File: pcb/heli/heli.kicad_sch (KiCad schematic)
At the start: 34 parts, among them J1 Batterie, J2 Debug, J3 Radio, Q1 IRLZ44N, U1 AZ1117-3.3, U2 STM32F103CBTx

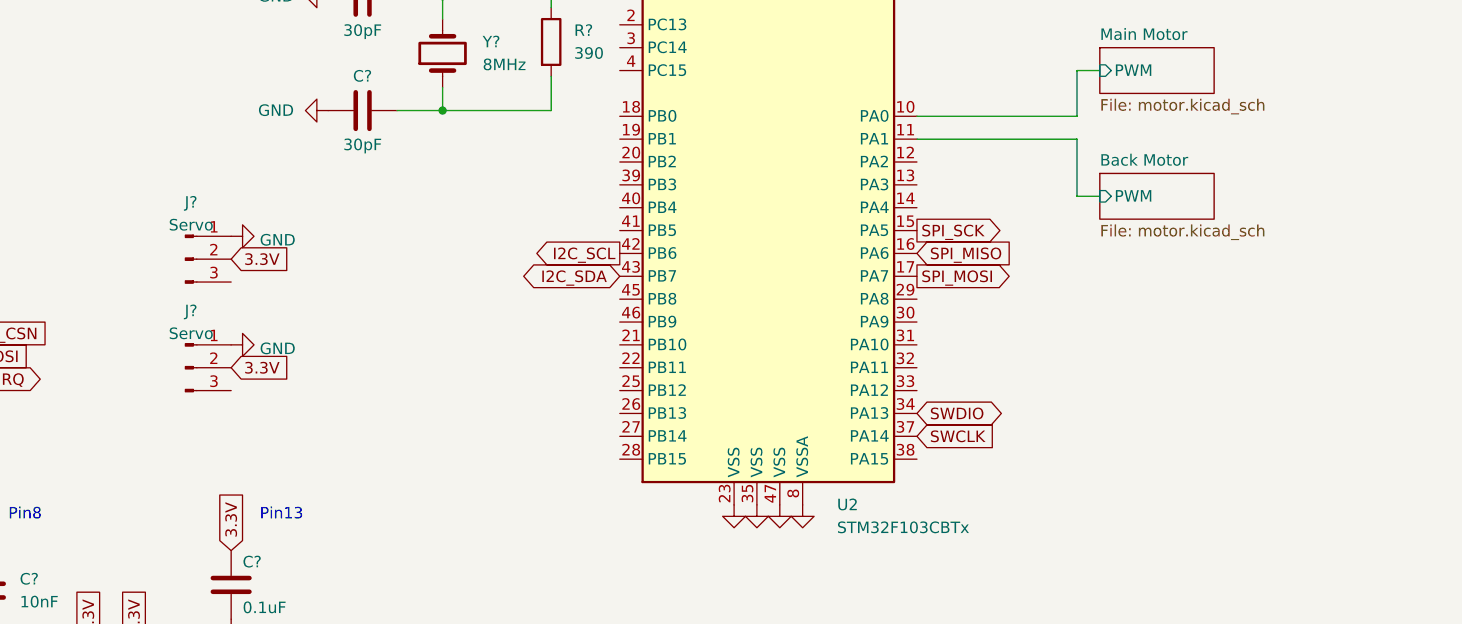
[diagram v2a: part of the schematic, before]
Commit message: 
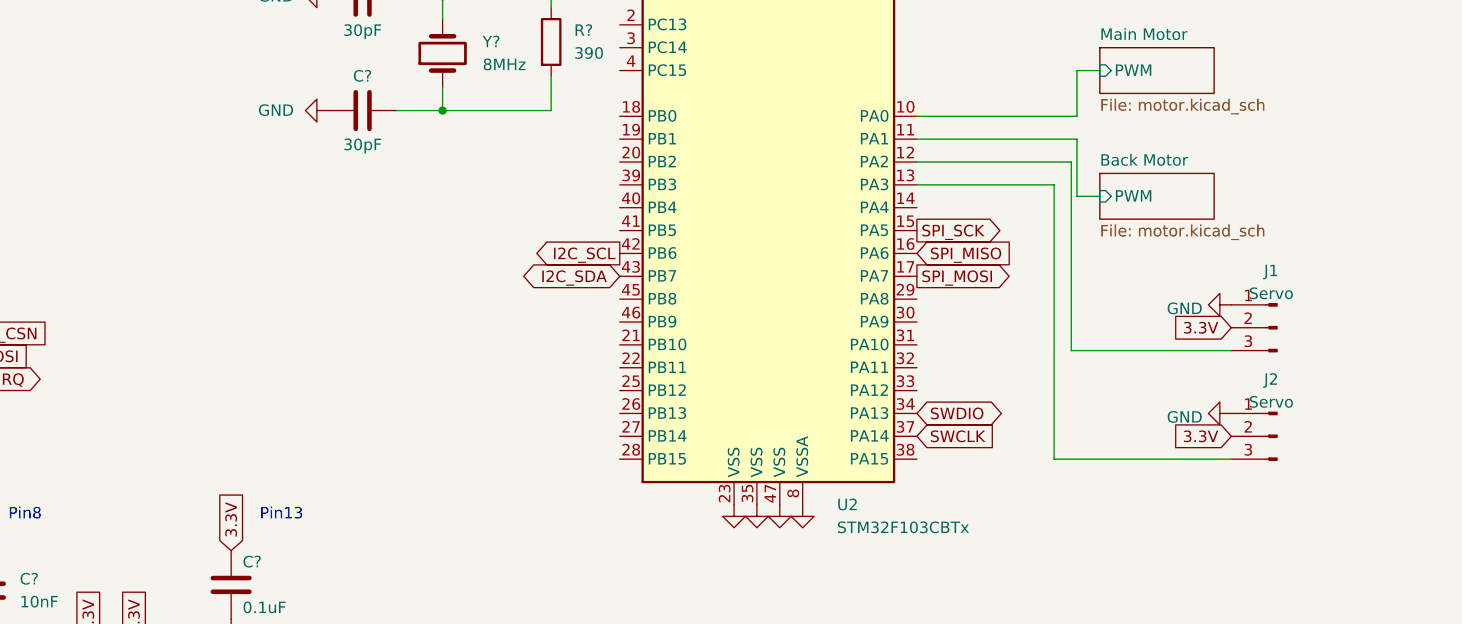
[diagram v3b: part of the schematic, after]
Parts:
- gave numbers to parts that had none: 2
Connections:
- net at U2.12 (PA2): now also J1.3 (Pin_3)
- net at U2.13 (PA3): now also J2.3 (Pin_3)
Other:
- moved on the sheet: J1, J2
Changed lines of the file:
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@@
+    (stroke (width 0) (type default) (color 0 0 0 0))
+  )
+  (wire (pts (xy 194.31 93.98) (xy 209.55 93.98))
     (stroke (width 0) (type default) (color 0 0 0 0))
   )
@@
     (stroke (width 0) (type default) (color 0 0 0 0))
   )
+  (wire (pts (xy 209.55 93.98) (xy 209.55 124.46))
+    (stroke (width 0) (type default) (color 0 0 0 0))
+  )
   (wire (pts (xy 38.1 55.88) (xy 45.72 55.88))
     (stroke (width 0) (type default) (color 0 0 0 0))
@@
     (stroke (width 0) (type default) (color 0 0 0 0))
   )
+  (wire (pts (xy 194.31 91.44) (xy 211.455 91.44))
+    (stroke (width 0) (type default) (color 0 0 0 0))
+  )
   (wire (pts (xy 245.11 39.37) (xy 245.11 34.29))
     (stroke (width 0) (type default) (color 0 0 0 0))
@@
     (stroke (width 0) (type default) (color 0 0 0 0))
   )
+  (wire (pts (xy 211.455 112.395) (xy 229.235 112.395))
+    (stroke (width 0) (type default) (color 0 0 0 0))
+  )
   (wire (pts (xy 104.14 36.83) (xy 113.03 36.83))
     (stroke (width 0) (type default) (color 0 0 0 0))
@@
     (stroke (width 0) (type default) (color 0 0 0 0))
   )
+  (wire (pts (xy 211.455 91.44) (xy 211.455 112.395))
+    (stroke (width 0) (type default) (color 0 0 0 0))
+  )
   (wire (pts (xy 141.605 75.565) (xy 141.605 73.025))
     (stroke (width 0) (type default) (color 0 0 0 0))
@@
   )
   (wire (pts (xy 33.02 67.31) (xy 29.21 67.31))
+    (stroke (width 0) (type default) (color 0 0 0 0))
+  )
+  (wire (pts (xy 209.55 124.46) (xy 229.235 124.46))
     (stroke (width 0) (type default) (color 0 0 0 0))
   )
@@
     )
   )
-  (global_label "3.3V" (shape input) (at 118.11 114.3 0) (fields_autoplaced)
-    (effects (font (size 1.27 1.27)) (justify left))
-    (property "Intersheet References" "${INTERSHEET_REFS}" (id 0) (at 124.6355 114.2206 0)
-      (effects (font (size 1.27 1.27)) (justify left) hide)
+  (global_label "3.3V" (shape input) (at 229.235 121.92 180) (fields_autoplaced)
+    (effects (font (size 1.27 1.27)) (justify right))
+    (property "Intersheet References" "${INTERSHEET_REFS}" (id 0) (at 222.7095 121.8406 0)
+      (effects (font (size 1.27 1.27)) (justify right) hide)
     )
   )
@@
     )
   )
-  (global_label "3.3V" (shape input) (at 118.11 102.235 0) (fields_autoplaced)
-    (effects (font (size 1.27 1.27)) (justify left))
-    (property "Intersheet References" "${INTERSHEET_REFS}" (id 0) (at 124.6355 102.1556 0)
-      (effects (font (size 1.27 1.27)) (justify left) hide)
+  (global_label "3.3V" (shape input) (at 229.235 109.855 180) (fields_autoplaced)
+    (effects (font (size 1.27 1.27)) (justify right))
+    (property "Intersheet References" "${INTERSHEET_REFS}" (id 0) (at 222.7095 109.7756 0)
+      (effects (font (size 1.27 1.27)) (justify right) hide)
     )
   )
@@
     (pin "9")
   )
-  (symbol (lib_id "Connector:Conn_01x03_Male") (at 113.03 114.3 0) (unit 1)
-    (in_bom yes) (on_board yes) (fields_autoplaced)
-    (property "Reference" "J?" (id 0) (at 113.665 107.984 0))
-    (property "Value" "Servo" (id 1) (at 113.665 110.5209 0))
-    (property "Footprint" "Connector_PinHeader_2.54mm:PinHeader_1x03_P2.54mm_Vertical" (id 2) (at 113.03 114.3 0)
-      (effects (font (size 1.27 1.27)) hide)
-    )
-    (property "Datasheet" "~" (id 3) (at 113.03 114.3 0)
+  (symbol (lib_id "Connector:Conn_01x03_Male") (at 234.315 121.92 0) (mirror y) (unit 1)
+    (in_bom yes) (on_board yes) (fields_autoplaced)
+    (property "Reference" "J2" (id 0) (at 233.68 115.604 0))
+    (property "Value" "Servo" (id 1) (at 233.68 118.1409 0))
+    (property "Footprint" "Connector_PinHeader_2.54mm:PinHeader_1x03_P2.54mm_Vertical" (id 2) (at 234.315 121.92 0)
+      (effects (font (size 1.27 1.27)) hide)
+    )
+    (property "Datasheet" "~" (id 3) (at 234.315 121.92 0)
       (effects (font (size 1.27 1.27)) hide)
     )
@@
     (pin "1")
   )
-  (symbol (lib_id "Connector:Conn_01x03_Male") (at 113.03 102.235 0) (unit 1)
-    (in_bom yes) (on_board yes) (fields_autoplaced)
-    (property "Reference" "J?" (id 0) (at 113.665 95.919 0))
-    (property "Value" "Servo" (id 1) (at 113.665 98.4559 0))
-    (property "Footprint" "Connector_PinHeader_2.54mm:PinHeader_1x03_P2.54mm_Vertical" (id 2) (at 113.03 102.235 0)
-      (effects (font (size 1.27 1.27)) hide)
-    )
-    (property "Datasheet" "~" (id 3) (at 113.03 102.235 0)
+  (symbol (lib_id "Connector:Conn_01x03_Male") (at 234.315 109.855 0) (mirror y) (unit 1)
+    (in_bom yes) (on_board yes) (fields_autoplaced)
+    (property "Reference" "J1" (id 0) (at 233.68 103.539 0))
+    (property "Value" "Servo" (id 1) (at 233.68 106.0759 0))
+    (property "Footprint" "Connector_PinHeader_2.54mm:PinHeader_1x03_P2.54mm_Vertical" (id 2) (at 234.315 109.855 0)
+      (effects (font (size 1.27 1.27)) hide)
+    )
+    (property "Datasheet" "~" (id 3) (at 234.315 109.855 0)
       (effects (font (size 1.27 1.27)) hide)
     )
@@
     (pin "2")
   )
-  (symbol (lib_id "power:GND") (at 118.11 99.695 90) (unit 1)
-    (in_bom yes) (on_board yes) (fields_autoplaced)
-    (property "Reference" "#PWR0130" (id 0) (at 124.46 99.695 0)
-      (effects (font (size 1.27 1.27)) hide)
-    )
-    (property "Value" "GND" (id 1) (at 121.285 100.1288 90)
+  (symbol (lib_id "power:GND") (at 229.235 107.315 270) (mirror x) (unit 1)
+    (in_bom yes) (on_board yes) (fields_autoplaced)
+    (property "Reference" "#PWR0130" (id 0) (at 222.885 107.315 0)
+      (effects (font (size 1.27 1.27)) hide)
+    )
+    (property "Value" "GND" (id 1) (at 226.06 107.7488 90)
       (effects (font (size 1.27 1.27)) (justify right))
     )
-    (property "Footprint" "" (id 2) (at 118.11 99.695 0)
-      (effects (font (size 1.27 1.27)) hide)
-    )
-    (property "Datasheet" "" (id 3) (at 118.11 99.695 0)
+    (property "Footprint" "" (id 2) (at 229.235 107.315 0)
+      (effects (font (size 1.27 1.27)) hide)
+    )
+    (property "Datasheet" "" (id 3) (at 229.235 107.315 0)
       (effects (font (size 1.27 1.27)) hide)
     )
@@
     (pin "2")
   )
-  (symbol (lib_id "power:GND") (at 118.11 111.76 90) (unit 1)
-    (in_bom yes) (on_board yes) (fields_autoplaced)
-    (property "Reference" "#PWR0129" (id 0) (at 124.46 111.76 0)
-      (effects (font (size 1.27 1.27)) hide)
-    )
-    (property "Value" "GND" (id 1) (at 121.285 112.1938 90)
+  (symbol (lib_id "power:GND") (at 229.235 119.38 270) (mirror x) (unit 1)
+    (in_bom yes) (on_board yes) (fields_autoplaced)
+    (property "Reference" "#PWR0129" (id 0) (at 222.885 119.38 0)
+      (effects (font (size 1.27 1.27)) hide)
+    )
+    (property "Value" "GND" (id 1) (at 226.06 119.8138 90)
       (effects (font (size 1.27 1.27)) (justify right))
     )
-    (property "Footprint" "" (id 2) (at 118.11 111.76 0)
-      (effects (font (size 1.27 1.27)) hide)
-    )
-    (property "Datasheet" "" (id 3) (at 118.11 111.76 0)
+    (property "Footprint" "" (id 2) (at 229.235 119.38 0)
+      (effects (font (size 1.27 1.27)) hide)
+    )
+    (property "Datasheet" "" (id 3) (at 229.235 119.38 0)
       (effects (font (size 1.27 1.27)) hide)
     )
@@
       (reference "D?") (unit 1) (value "LED") (footprint "LED_SMD:LED_0603_1608Metric")
     )
+    (path "/6a616114-ec84-4df9-9c86-6292a01164f6"
+      (reference "J1") (unit 1) (value "Servo") (footprint "Connector_PinHeader_2.54mm:PinHeader_1x03_P2.54mm_Vertical")
+    )
     (path "/7343ee5a-7884-4dc9-ac03-cc5d5c203894"
       (reference "J1") (unit 1) (value "Batterie") (footprint "Connector_PinHeader_2.54mm:PinHeader_1x02_P2.54mm_Horizontal")
     )
+    (path "/629d9c9a-835c-4513-b36f-084bde0489e8"
+      (reference "J2") (unit 1) (value "Servo") (footprint "Connector_PinHeader_2.54mm:PinHeader_1x03_P2.54mm_Vertical")
+    )
     (path "/a572e332-5d04-4c16-ab49-7a7eb34c0212"
       (reference "J2") (unit 1) (value "Debug") (footprint "Connector_PinHeader_2.54mm:PinHeader_1x05_P2.54mm_Vertical")
@@
       (reference "J3") (unit 1) (value "Radio") (footprint "Connector_PinHeader_2.54mm:PinHeader_2x04_P2.54mm_Vertical")
     )
-    (path "/629d9c9a-835c-4513-b36f-084bde0489e8"
-      (reference "J?") (unit 1) (value "Servo") (footprint "Connector_PinHeader_2.54mm:PinHeader_1x03_P2.54mm_Vertical")
-    )
-    (path "/6a616114-ec84-4df9-9c86-6292a01164f6"
-      (reference "J?") (unit 1) (value "Servo") (footprint "Connector_PinHeader_2.54mm:PinHeader_1x03_P2.54mm_Vertical")
-    )
     (path "/c5583cdf-ca59-48f7-a91f-20c1806ad1c1/ea2bd08c-49e2-43b8-8c1f-a2b101dfb062"

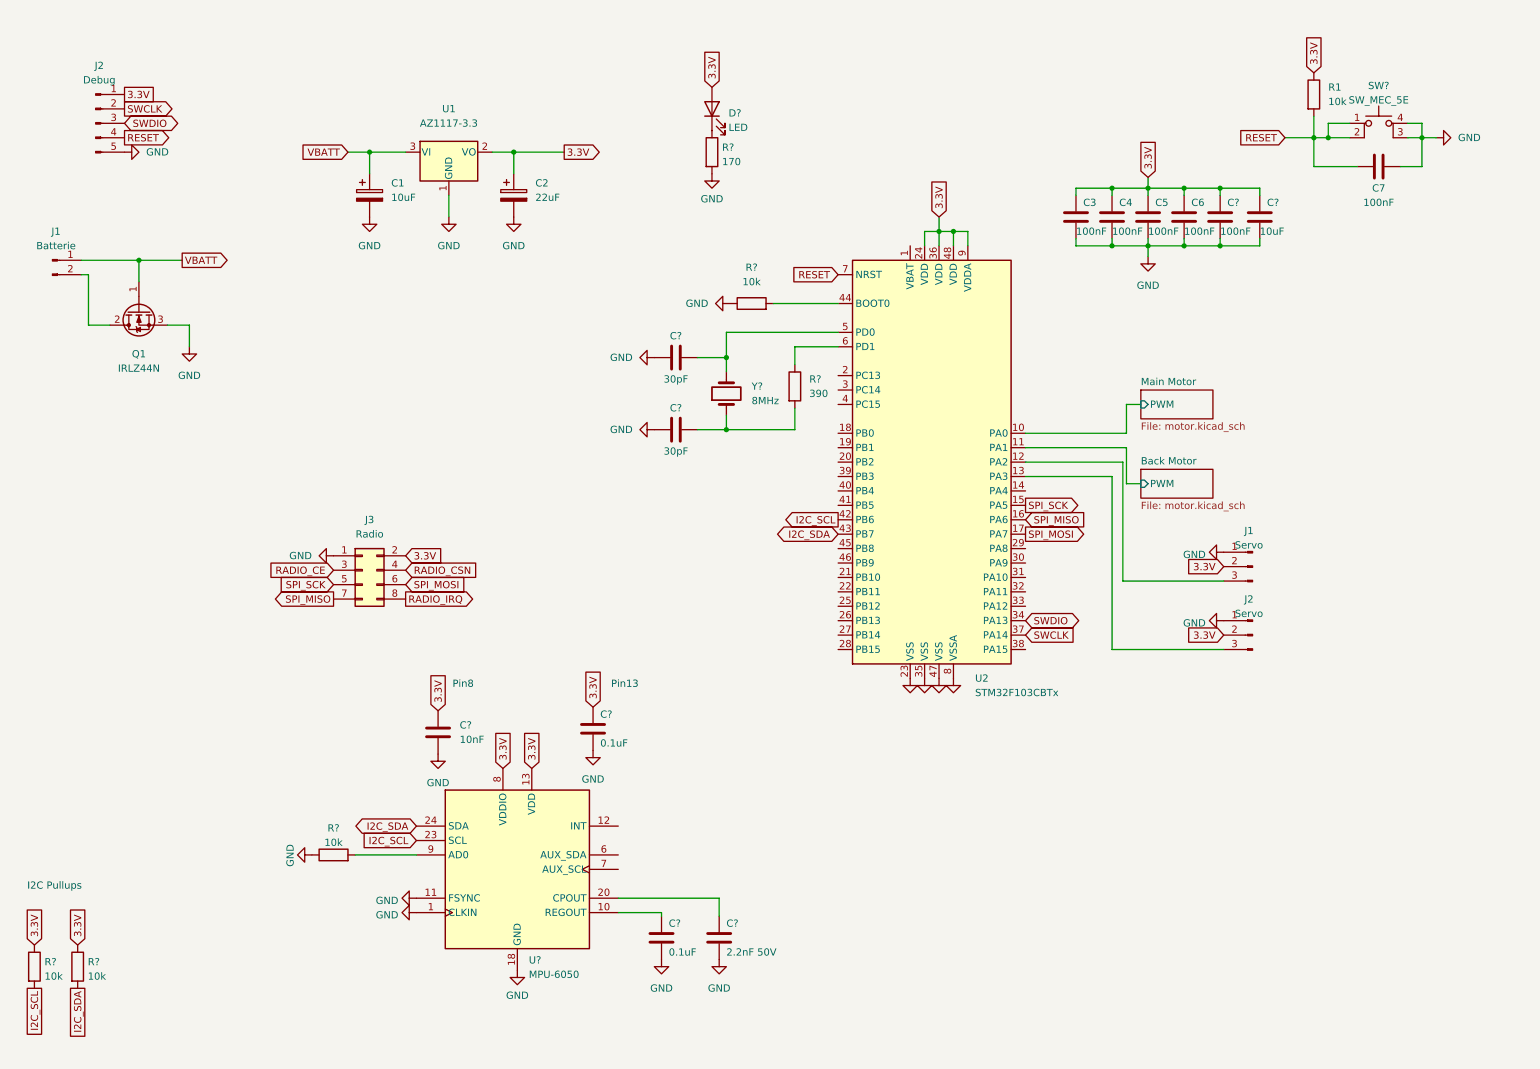
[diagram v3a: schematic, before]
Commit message: 
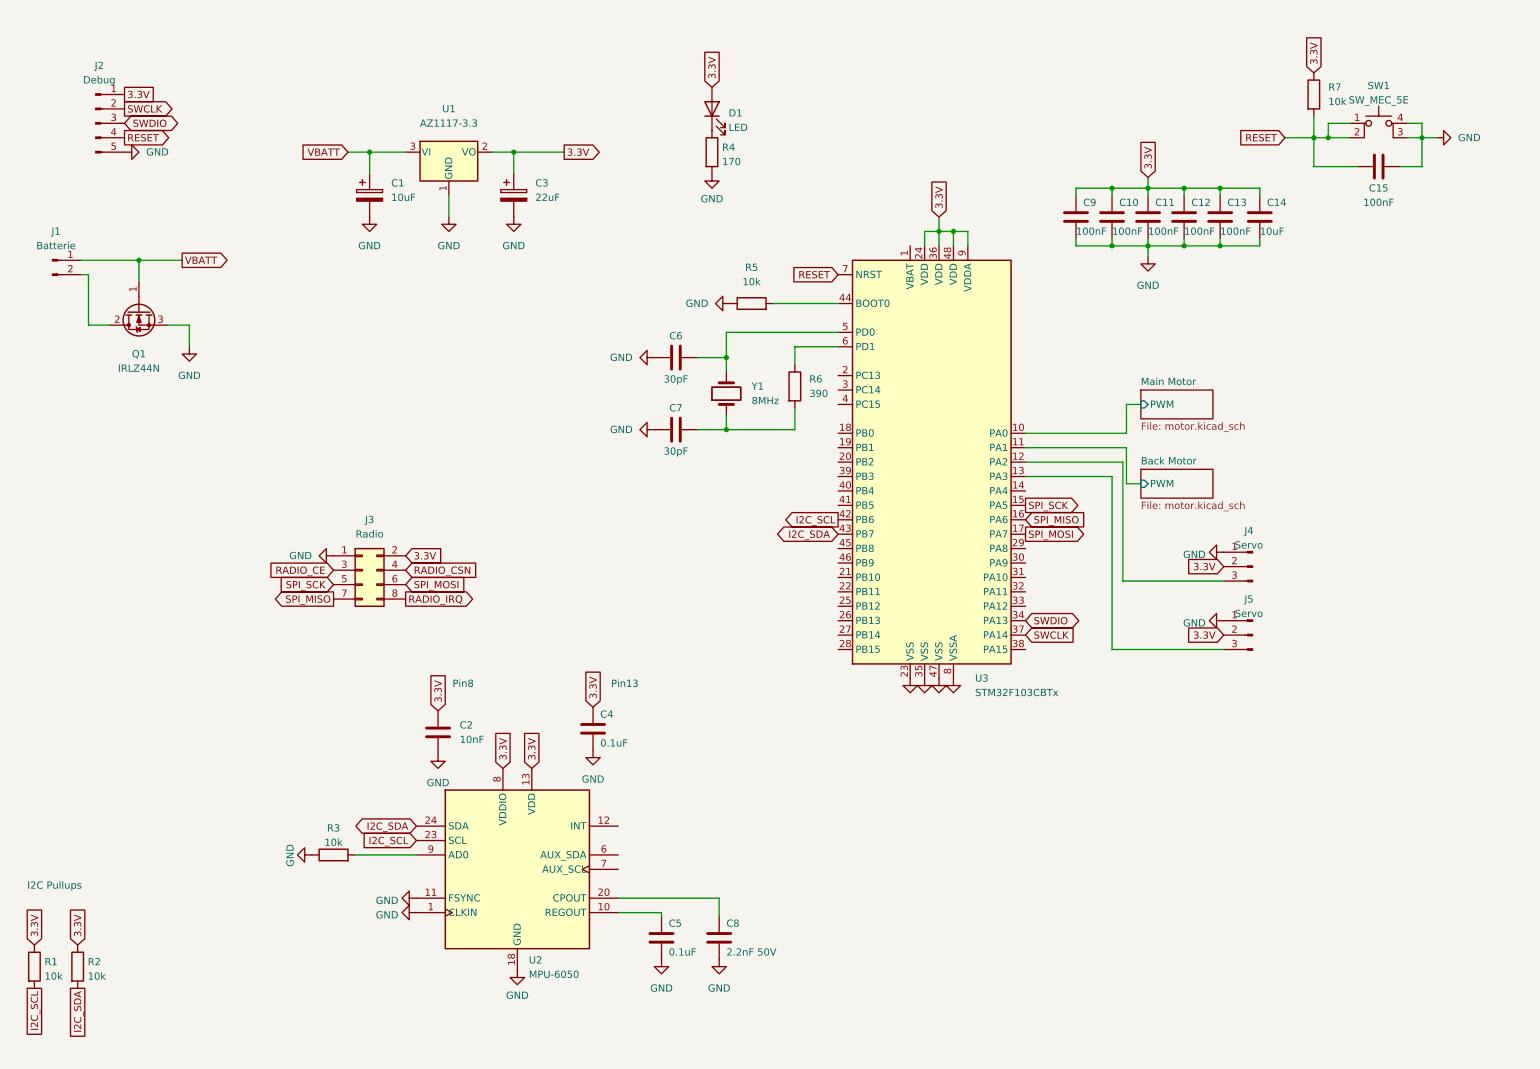
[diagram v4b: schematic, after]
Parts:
- J1: footprint Connector_PinHeader_2.54mm:PinHeader_1x02_P2.54mm_Horizontal -> Connector_PinHeader_2.54mm:PinHeader_1x02_P2.54mm_Vertical
- gave numbers to parts that had none: 18
- renumbered C4 to C10, C5 to C11, C6 to C12, C7 to C15, C2 to C3, C3 to C9, J1 to J4, J2 to J5, R1 to R7, U2 to U3
